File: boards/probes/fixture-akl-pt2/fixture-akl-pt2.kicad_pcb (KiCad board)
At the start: 4 copper layers, 25 x 25.2 mm, 3 parts, among them J1 901-10511-3, J2 901-10511-3

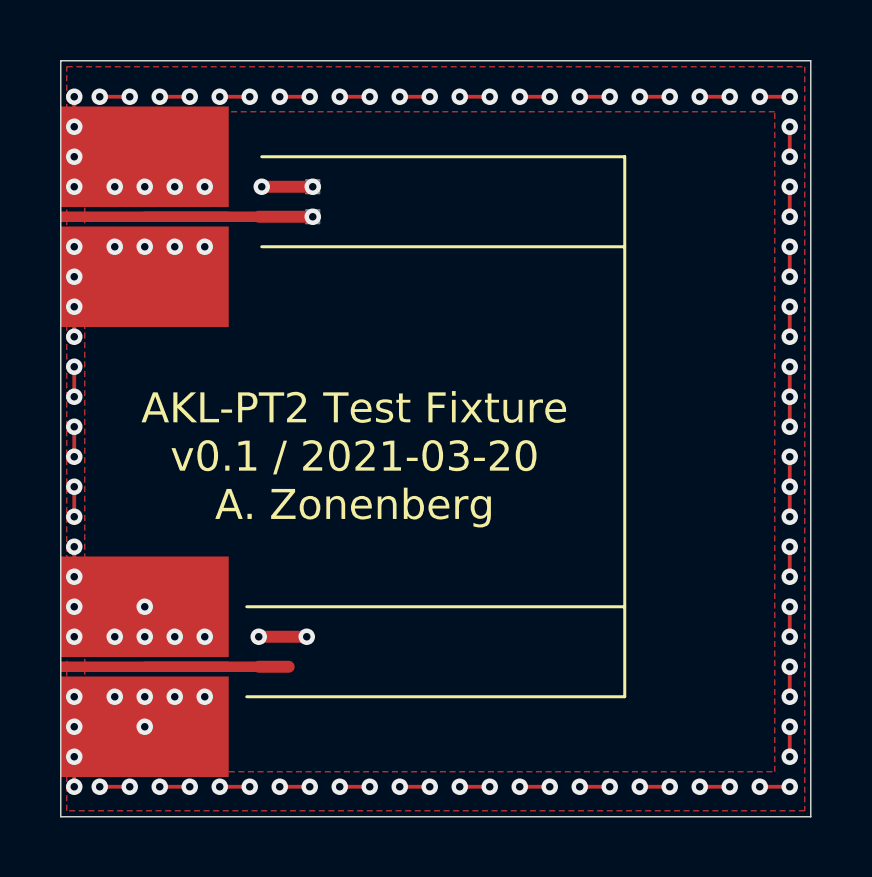
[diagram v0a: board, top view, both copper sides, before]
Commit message: Moved terminating resistor so we don't have vias in pads
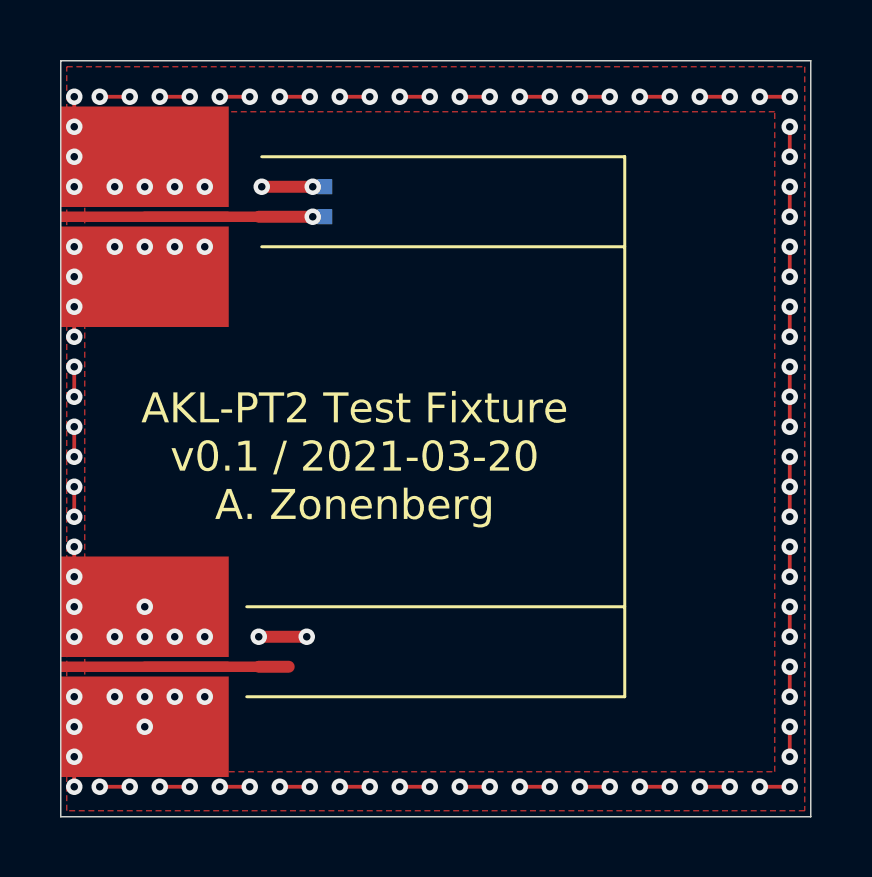
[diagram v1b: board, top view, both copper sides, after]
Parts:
- moved R1 0.40 mm to (38.0, 36.5)
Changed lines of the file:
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@@
     (thickness 1.6)
     (drawings 10)
-    (tracks 241)
+    (tracks 243)
     (zones 0)
     (modules 3)
@@
   )
   (module azonenberg_pcb:EIA_0402_RES_NOSILK_FLIPCHIP (layer B.Cu)
-    (at 37.6 36.5 90)
+    (at 38 36.5 90)
     (solder_paste_margin -0.06)
     (fp_text reference R1 (at 0 -1.5 90) (layer B.SilkS) hide
@@
   (segment (start 32 53) (end 31 53) (width 0.125) (layer In1.Cu) (net 1))
   (segment (start 31 53) (end 30 53) (width 0.125) (layer F.Cu) (net 1))
+  (segment (start 38 36) (end 37.6 36) (width 0.4) (layer B.Cu) (net 1))
   (segment (start 32 37) (end 35.8 37) (width 0.35) (layer F.Cu) (net 2))
   (segment (start 35.8 37) (end 37.4 37) (width 0.4) (layer F.Cu) (net 2))
   (via (at 37.6 37) (size 0.55) (drill 0.25) (layers F.Cu B.Cu) (net 2))
+  (segment (start 38 37) (end 37.6 37) (width 0.4) (layer B.Cu) (net 2))
   (segment (start 32 52) (end 35.8 52) (width 0.35) (layer F.Cu) (net 3))
   (segment (start 35.8 52) (end 36.8 52) (width 0.4) (layer F.Cu) (net 3))
